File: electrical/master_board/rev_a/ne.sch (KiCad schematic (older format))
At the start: 8 parts, among them CN105 BRIDGE_NE_OUTER;2xM1x1+M1x5, CN60 HCSR04;F1x4H

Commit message: The four corner boards ne/nw/se/sw are now zoned.
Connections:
- net labels added: GND
- wire segments 0 -> 1
- no-connect marks 12 -> 11
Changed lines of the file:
@@
 	1    0    0    -1
 $EndComp
-NoConn ~ 3000 1500
+NoConn ~ 3400 1500
 NoConn ~ 3000 1900
 NoConn ~ 3000 2300
@@
 NoConn ~ 3000 2600
 NoConn ~ 3000 2700
-NoConn ~ 3250 800
+Wire Wire Line
+	3000 1500 3400 1500
+Text Label 3100 1500 0    50   ~ 0
+GND
 $EndSCHEMATC

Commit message: Got NE PCB done.
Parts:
- removed CN105: BRIDGE_NE_OUTER;2xM1x1+M1x5, HR2:BRIDGE_NE_OUTER_2xM1x1+M1x5, symbol HR2:BRIDGE_NE_OUTER;2xM1x1+M1x5
- added CN105: BRIDGE_NE_OUTER;3xM1x1+M1x5, HR2:BRIDGE_NE_OUTER_3xM1x1+M1x5, symbol HR2:BRIDGE_NE_OUTER;3xM1x1+M1x5
- added Q1, Q2, Q3: 2N7000;SOT23, Package_TO_SOT_SMD:SOT-23, symbol Transistor_FET:2N7000
- added R1, R2, R3, R4, R5, R6, R7, R8, R9: 330Ω;1608, Resistor_SMD:R_0603_1608Metric, symbol Device:R_US
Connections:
- net labels added: 5V, 9V, ECHO, LED1, LED2, LED3, TRIG
- wire segments 1 -> 71
- no-connect marks 11 -> 0
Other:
- note added: "Note: CN101 is actually 4 connectors that are treated one to keep\n them properly aligned with C102."
- note added: "Notes:\n1. GRNRA = Green Right Angle Green\n2. Nominal Part:\n Mfg Part #: TLPG5600\n Digi-Key part #: TLPG5600-ND\n Forward Voltage Drop: 2.4V\n Absolute max. current: 200mA\n Target maximum current: I=60mA\n Resistor: R = (9V - 2.4V) / 75mA = 6.6V / .060A = 110Ω\n Watts: W = I**2*R = (.060 * .060) * 110 = .396W ~=.4W\n Use 3 x 330Ω in parallel to get 110Ω\n Watts per resistor: Wr = .4W / 3 = .1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"
- moved on the sheet: CN60, D1

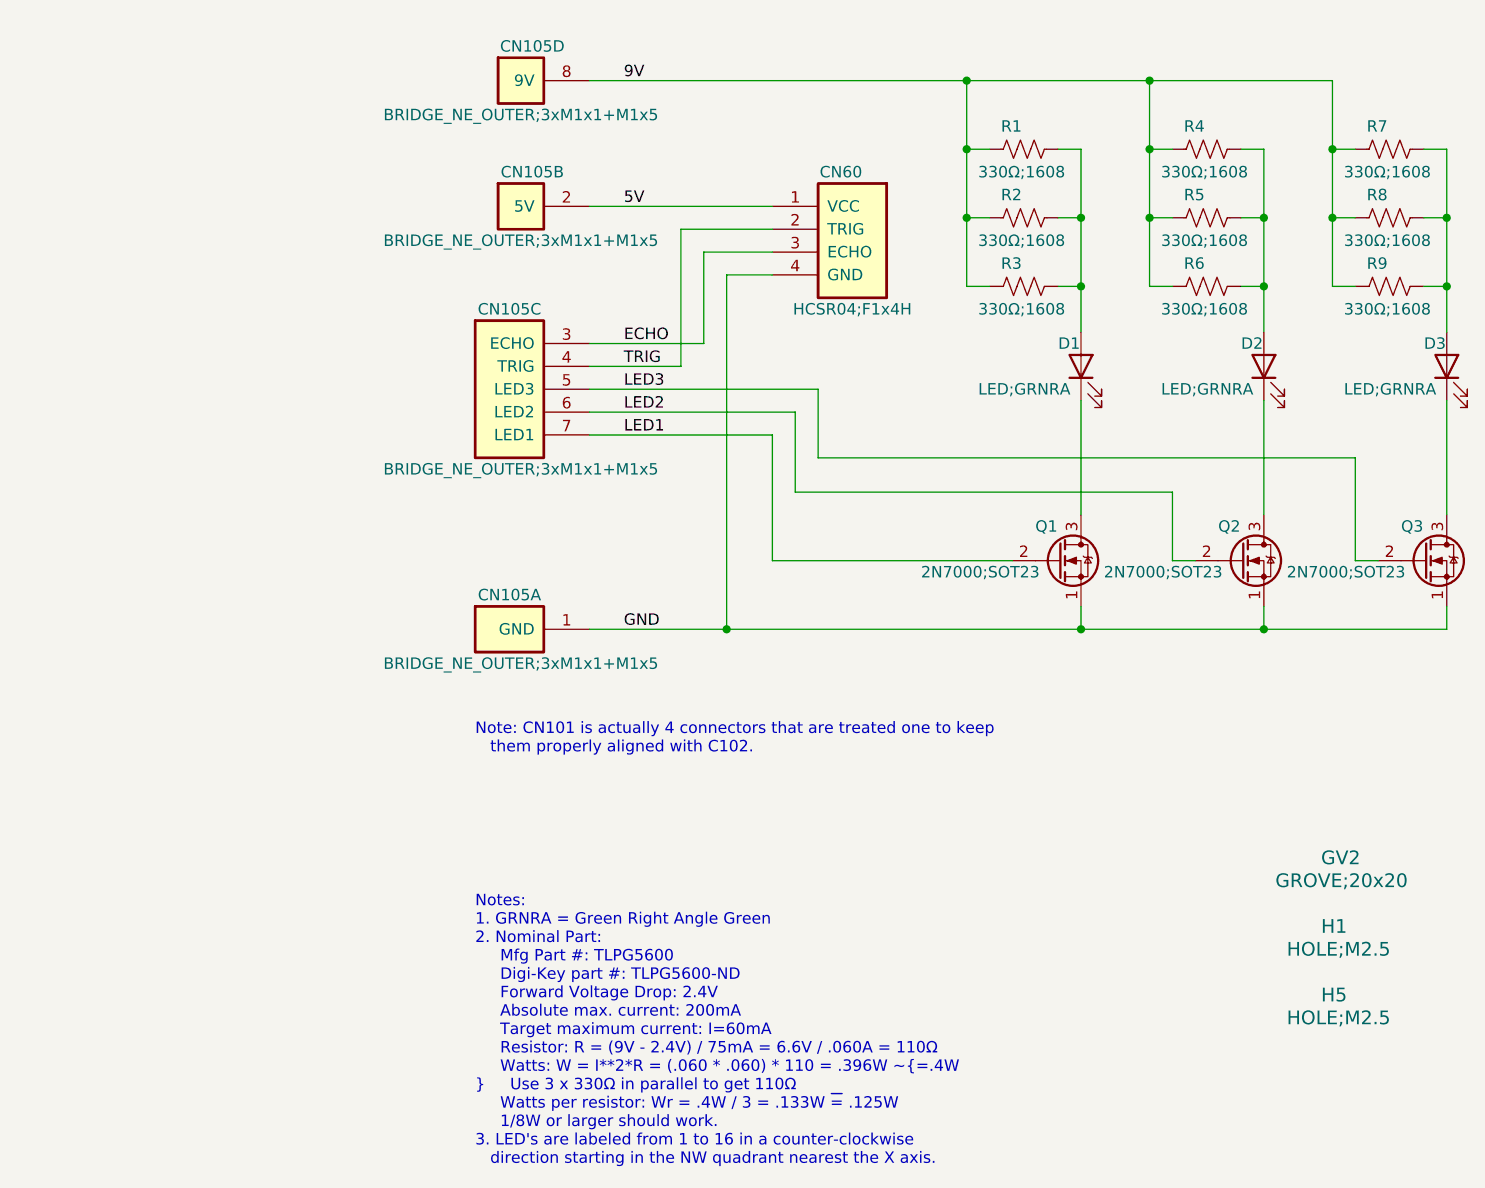
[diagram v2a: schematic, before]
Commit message: Linked the NE/NW/SE/SW sheets to master_board.
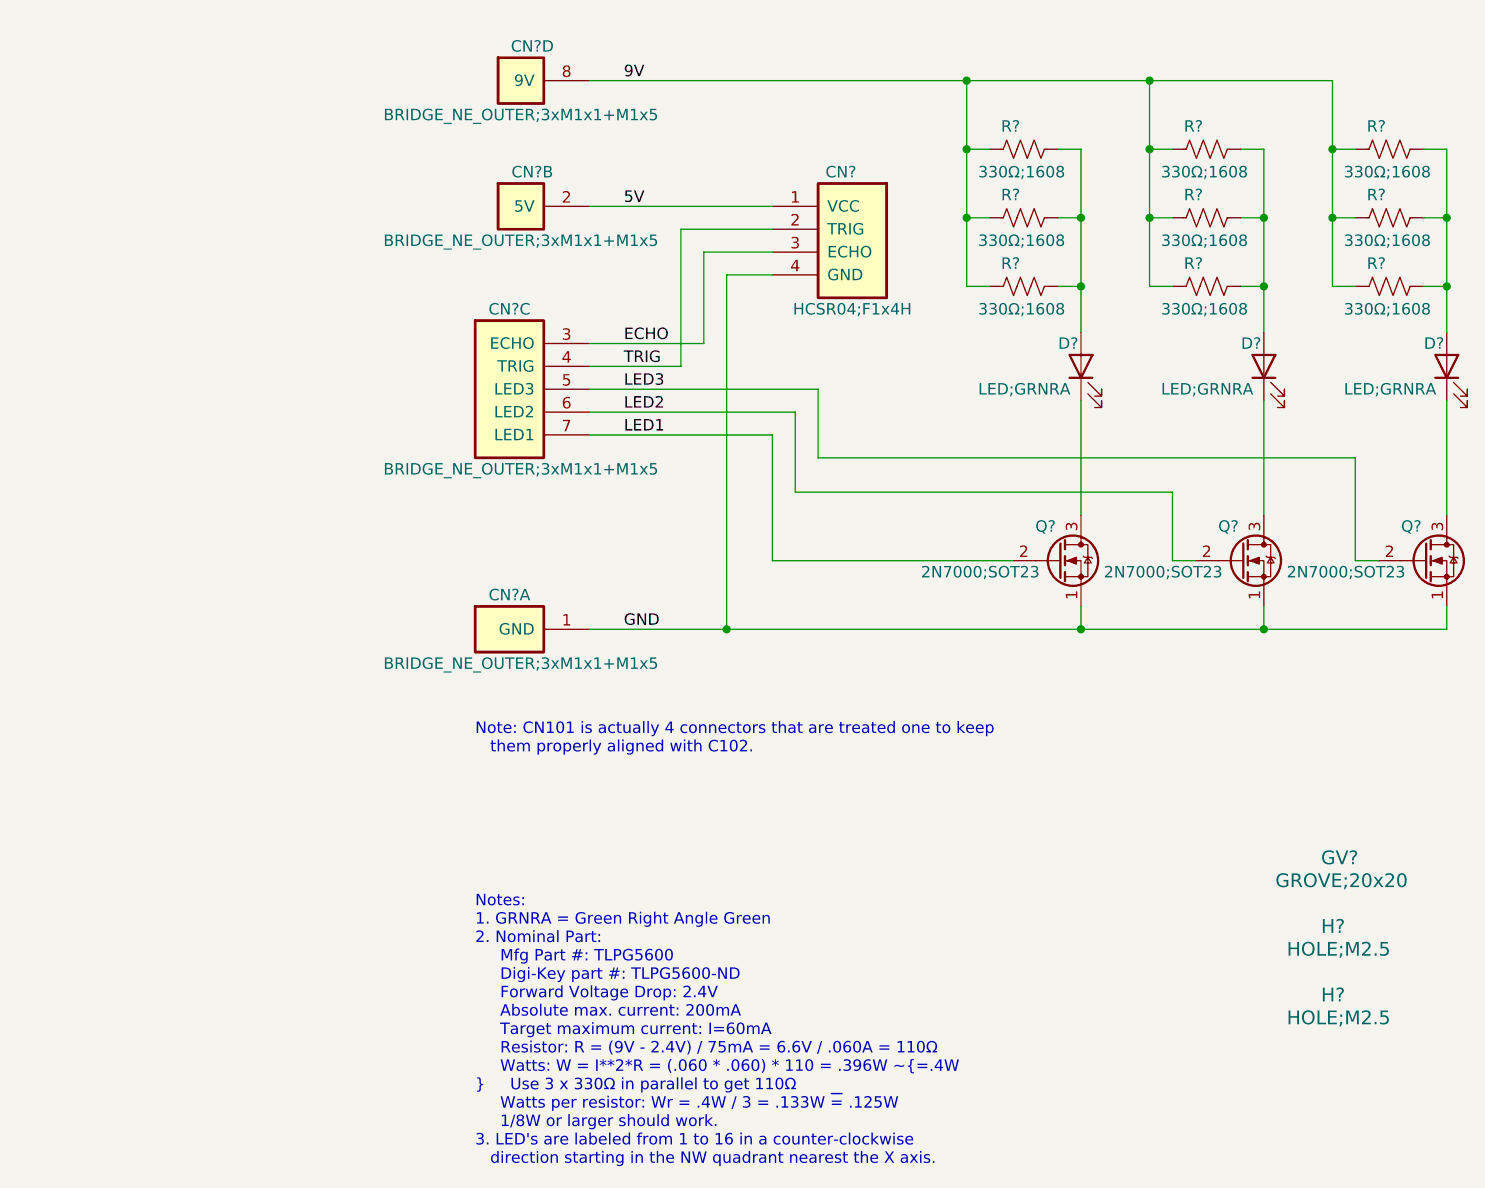
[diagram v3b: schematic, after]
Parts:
- renumbered CN60 to CN?, CN105 to CN?, D1 to D?, D2 to D?, D3 to D?, GV2 to GV?, H5 to H?, H1 to H?, Q1 to Q?, Q2 to Q?, Q3 to Q?, R9 to R?, R8 to R?, R7 to R?, R6 to R?, R5 to R?, R4 to R?, R3 to R?, R2 to R?, R1 to R?
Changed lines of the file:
@@
 $Descr A 11000 8500
 encoding utf-8
-Sheet 1 1
+Sheet 9 12
 Title "HR2 NE PCB"
 Date "2020-06-13"
@@
 $EndDescr
 $Comp
-L HR2:HCSR04H;F1X4 CN60
+L HR2:HCSR04H;F1X4 CN?
 U 1 1 5EE6BF38
 P 5500 1600
-F 0 "CN60" H 5900 1750 50  0000 C CNN
+F 0 "CN?" H 5900 1750 50  0000 C CNN
 F 1 "HCSR04;F1x4H" H 5850 1150 50  0000 C CNN
 F 2 "HR2:HCSR04_F1x4H" H 5700 1650 60  0001 L CNN
@@
 $EndComp
 $Comp
-L HR2:HOLE;M2.5 H5
+L HR2:HOLE;M2.5 H?
 U 1 1 5F2F7E7C
 P 7300 5100
-F 0 "H5" H 7200 5150 60  0000 L CNN
+F 0 "H?" H 7200 5150 60  0000 L CNN
 F 1 "HOLE;M2.5" H 7050 5050 60  0000 L CNN
 F 2 "MountingHole:MountingHole_2.7mm_M2.5" H 7500 5150 60  0001 L CNN
@@
 $EndComp
 $Comp
-L HR2:HOLE;M2.5 H1
+L HR2:HOLE;M2.5 H?
 U 1 1 5F2F85AA
 P 7300 4800
-F 0 "H1" H 7200 4850 60  0000 L CNN
+F 0 "H?" H 7200 4850 60  0000 L CNN
 F 1 "HOLE;M2.5" H 7050 4750 60  0000 L CNN
 F 2 "MountingHole:MountingHole_2.7mm_M2.5" H 7500 4850 60  0001 L CNN
@@
 $EndComp
 $Comp
-L HR2:GROVE;20x20 GV2
+L HR2:GROVE;20x20 GV?
 U 1 1 5F2F9731
 P 7300 4500
-F 0 "GV2" H 7200 4550 60  0000 L CNN
+F 0 "GV?" H 7200 4550 60  0000 L CNN
 F 1 "GROVE;20x20" H 7000 4450 60  0000 L CNN
 F 2 "HR2:GROVE20x20" H 7500 4550 60  0001 L CNN
@@
 $EndComp
 $Comp
-L Device:LED D1
+L Device:LED D?
 U 1 1 5F30B259
 P 6150 2300
-F 0 "D1" V 6250 2400 50  0000 R CNN
+F 0 "D?" V 6250 2400 50  0000 R CNN
 F 1 "LED;GRNRA" V 6050 2750 50  0000 R CNN
 F 2 "HR2:LED_GRNRA" H 6150 2300 50  0001 C CNN
@@
 GND
 $Comp
-L Transistor_FET:2N7000 Q1
+L Transistor_FET:2N7000 Q?
 U 1 1 5F4294E7
 P 6050 3150
-F 0 "Q1" H 5950 3300 50  0000 L CNN
+F 0 "Q?" H 5950 3300 50  0000 L CNN
 F 1 "2N7000;SOT23" H 5450 3100 50  0000 L CNN
 F 2 "Package_TO_SOT_SMD:SOT-23" H 6250 3075 50  0001 L CIN
@@
 $EndComp
 $Comp
-L Device:R_US R9
+L Device:R_US R?
 U 1 1 5F429CFC
 P 7500 1950
-F 0 "R9" V 7400 1850 50  0000 L CNN
+F 0 "R?" V 7400 1850 50  0000 L CNN
 F 1 "330Ω;1608" V 7600 1750 50  0000 L CNN
 F 2 "Resistor_SMD:R_0603_1608Metric" V 7540 1940 50  0001 C CNN
@@
 Notes:\n1. GRNRA = Green Right Angle Green\n2. Nominal Part:\n     Mfg Part #: TLPG5600\n     Digi-Key part #: TLPG5600-ND\n     Forward Voltage Drop: 2.4V\n     Absolute max. current: 200mA\n     Target maximum current: I=60mA\n     Resistor: R = (9V - 2.4V) / 75mA = 6.6V / .060A = 110Ω\n     Watts: W = I**2*R = (.060 * .060) * 110 = .396W ~=.4W\n     Use 3 x 330Ω in parallel to get 110Ω\n     Watts per resistor: Wr = .4W / 3 = .133W ~= .125W\n     1/8W or larger should work.\n3. LED's are labeled from 1 to 16 in a counter-clockwise\n   direction starting in the NW quadrant nearest the X axis.
 $Comp
-L Device:R_US R8
+L Device:R_US R?
 U 1 1 5F42F445
 P 7500 1650
-F 0 "R8" V 7400 1550 50  0000 L CNN
+F 0 "R?" V 7400 1550 50  0000 L CNN
 F 1 "330Ω;1608" V 7600 1450 50  0000 L CNN
 F 2 "Resistor_SMD:R_0603_1608Metric" V 7540 1640 50  0001 C CNN
@@
 $EndComp
 $Comp
-L Device:R_US R7
+L Device:R_US R?
 U 1 1 5F42F75B
 P 7500 1350
-F 0 "R7" V 7400 1250 50  0000 L CNN
+F 0 "R?" V 7400 1250 50  0000 L CNN
 F 1 "330Ω;1608" V 7600 1150 50  0000 L CNN
 F 2 "Resistor_SMD:R_0603_1608Metric" V 7540 1340 50  0001 C CNN
@@
 	6150 2950 6150 2450
 $Comp
-L Device:LED D2
+L Device:LED D?
 U 1 1 5F436F00
 P 6950 2300
-F 0 "D2" V 7050 2400 50  0000 R CNN
+F 0 "D?" V 7050 2400 50  0000 R CNN
 F 1 "LED;GRNRA" V 6850 2750 50  0000 R CNN
 F 2 "HR2:LED_GRNRA" H 6950 2300 50  0001 C CNN
@@
 $EndComp
 $Comp
-L Transistor_FET:2N7000 Q2
+L Transistor_FET:2N7000 Q?
 U 1 1 5F436F0A
 P 6850 3150
-F 0 "Q2" H 6750 3300 50  0000 L CNN
+F 0 "Q?" H 6750 3300 50  0000 L CNN
 F 1 "2N7000;SOT23" H 6250 3100 50  0000 L CNN
 F 2 "Package_TO_SOT_SMD:SOT-23" H 7050 3075 50  0001 L CIN
@@
 $EndComp
 $Comp
-L Device:R_US R6
+L Device:R_US R?
 U 1 1 5F436F14
 P 6700 1950
-F 0 "R6" V 6600 1850 50  0000 L CNN
+F 0 "R?" V 6600 1850 50  0000 L CNN
 F 1 "330Ω;1608" V 6800 1750 50  0000 L CNN
 F 2 "Resistor_SMD:R_0603_1608Metric" V 6740 1940 50  0001 C CNN
@@
 $EndComp
 $Comp
-L Device:R_US R5
+L Device:R_US R?
 U 1 1 5F436F1E
 P 6700 1650
-F 0 "R5" V 6600 1550 50  0000 L CNN
+F 0 "R?" V 6600 1550 50  0000 L CNN
 F 1 "330Ω;1608" V 6800 1450 50  0000 L CNN
 F 2 "Resistor_SMD:R_0603_1608Metric" V 6740 1640 50  0001 C CNN
@@
 $EndComp
 $Comp
-L Device:R_US R4
+L Device:R_US R?
 U 1 1 5F436F28
 P 6700 1350
-F 0 "R4" V 6600 1250 50  0000 L CNN
+F 0 "R?" V 6600 1250 50  0000 L CNN
 F 1 "330Ω;1608" V 6800 1150 50  0000 L CNN
 F 2 "Resistor_SMD:R_0603_1608Metric" V 6740 1340 50  0001 C CNN
@@
 Connection ~ 6450 1350
 $Comp
-L Device:LED D3
+L Device:LED D?
 U 1 1 5F43BB9D
 P 7750 2300
-F 0 "D3" V 7850 2400 50  0000 R CNN
+F 0 "D?" V 7850 2400 50  0000 R CNN
 F 1 "LED;GRNRA" V 7650 2750 50  0000 R CNN
 F 2 "HR2:LED_GRNRA" H 7750 2300 50  0001 C CNN
@@
 $EndComp
 $Comp
-L Device:R_US R3
+L Device:R_US R?
 U 1 1 5F43BBB1
 P 5900 1950
-F 0 "R3" V 5800 1850 50  0000 L CNN
+F 0 "R?" V 5800 1850 50  0000 L CNN
 F 1 "330Ω;1608" V 6000 1750 50  0000 L CNN
 F 2 "Resistor_SMD:R_0603_1608Metric" V 5940 1940 50  0001 C CNN
@@
 $EndComp
 $Comp
-L Device:R_US R2
+L Device:R_US R?
 U 1 1 5F43BBBB
 P 5900 1650
-F 0 "R2" V 5800 1550 50  0000 L CNN
+F 0 "R?" V 5800 1550 50  0000 L CNN
 F 1 "330Ω;1608" V 6000 1450 50  0000 L CNN
 F 2 "Resistor_SMD:R_0603_1608Metric" V 5940 1640 50  0001 C CNN
@@
 $EndComp
 $Comp
-L Device:R_US R1
+L Device:R_US R?
 U 1 1 5F43BBC5
 P 5900 1350
-F 0 "R1" V 5800 1250 50  0000 L CNN
+F 0 "R?" V 5800 1250 50  0000 L CNN
 F 1 "330Ω;1608" V 6000 1150 50  0000 L CNN
 F 2 "Resistor_SMD:R_0603_1608Metric" V 5940 1340 50  0001 C CNN
@@
 	4000 1600 4800 1600
 $Comp
-L Transistor_FET:2N7000 Q3
+L Transistor_FET:2N7000 Q?
 U 1 1 5F43BBA7
 P 7650 3150
-F 0 "Q3" H 7550 3300 50  0000 L CNN
+F 0 "Q?" H 7550 3300 50  0000 L CNN
 F 1 "2N7000;SOT23" H 7050 3100 50  0000 L CNN
 F 2 "Package_TO_SOT_SMD:SOT-23" H 7850 3075 50  0001 L CIN
@@
 Note: CN101 is actually 4 connectors that are treated one to keep\n   them properly aligned with C102.
 $Comp
-L HR2:BRIDGE_NE_OUTER;3xM1x1+M1x5 CN105
+L HR2:BRIDGE_NE_OUTER;3xM1x1+M1x5 CN?
 U 1 1 5F442084
 P 3300 3450
-F 0 "CN105" H 3650 3600 50  0000 C CNN
+F 0 "CN?" H 3650 3600 50  0000 C CNN
 F 1 "BRIDGE_NE_OUTER;3xM1x1+M1x5" H 3700 3300 50  0000 C CNN
 F 2 "HR2:BRIDGE_NE_OUTER_3xM1x1+M1x5" H 3500 3500 60  0001 L CNN
@@
 $EndComp
 $Comp
-L HR2:BRIDGE_NE_OUTER;3xM1x1+M1x5 CN105
+L HR2:BRIDGE_NE_OUTER;3xM1x1+M1x5 CN?
 U 2 1 5F44303C
 P 3400 1600
-F 0 "CN105" H 3750 1750 50  0000 C CNN
+F 0 "CN?" H 3750 1750 50  0000 C CNN
 F 1 "BRIDGE_NE_OUTER;3xM1x1+M1x5" H 3700 1450 50  0000 C CNN
 F 2 "HR2:BRIDGE_NE_OUTER_3xM1x1+M1x5" H 3600 1650 60  0001 L CNN
@@
 $EndComp
 $Comp
-L HR2:BRIDGE_NE_OUTER;3xM1x1+M1x5 CN105
+L HR2:BRIDGE_NE_OUTER;3xM1x1+M1x5 CN?
 U 4 1 5F44482A
 P 3400 1050
-F 0 "CN105" H 3750 1200 50  0000 C CNN
+F 0 "CN?" H 3750 1200 50  0000 C CNN
 F 1 "BRIDGE_NE_OUTER;3xM1x1+M1x5" H 3700 900 50  0000 C CNN
 F 2 "HR2:BRIDGE_NE_OUTER_3xM1x1+M1x5" H 3600 1100 60  0001 L CNN
@@
 $EndComp
 $Comp
-L HR2:BRIDGE_NE_OUTER;3xM1x1+M1x5 CN105
+L HR2:BRIDGE_NE_OUTER;3xM1x1+M1x5 CN?
 U 3 1 5F445670
 P 3300 2200
-F 0 "CN105" H 3650 2350 50  0000 C CNN
+F 0 "CN?" H 3650 2350 50  0000 C CNN
 F 1 "BRIDGE_NE_OUTER;3xM1x1+M1x5" H 3700 1650 50  0000 C CNN
 F 2 "HR2:BRIDGE_NE_OUTER_3xM1x1+M1x5" H 3500 2250 60  0001 L CNN
